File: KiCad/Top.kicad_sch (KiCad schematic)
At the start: 7 parts, among them U143 PZ254V-11-04P_C2691448, U144 HS96L03W2C03

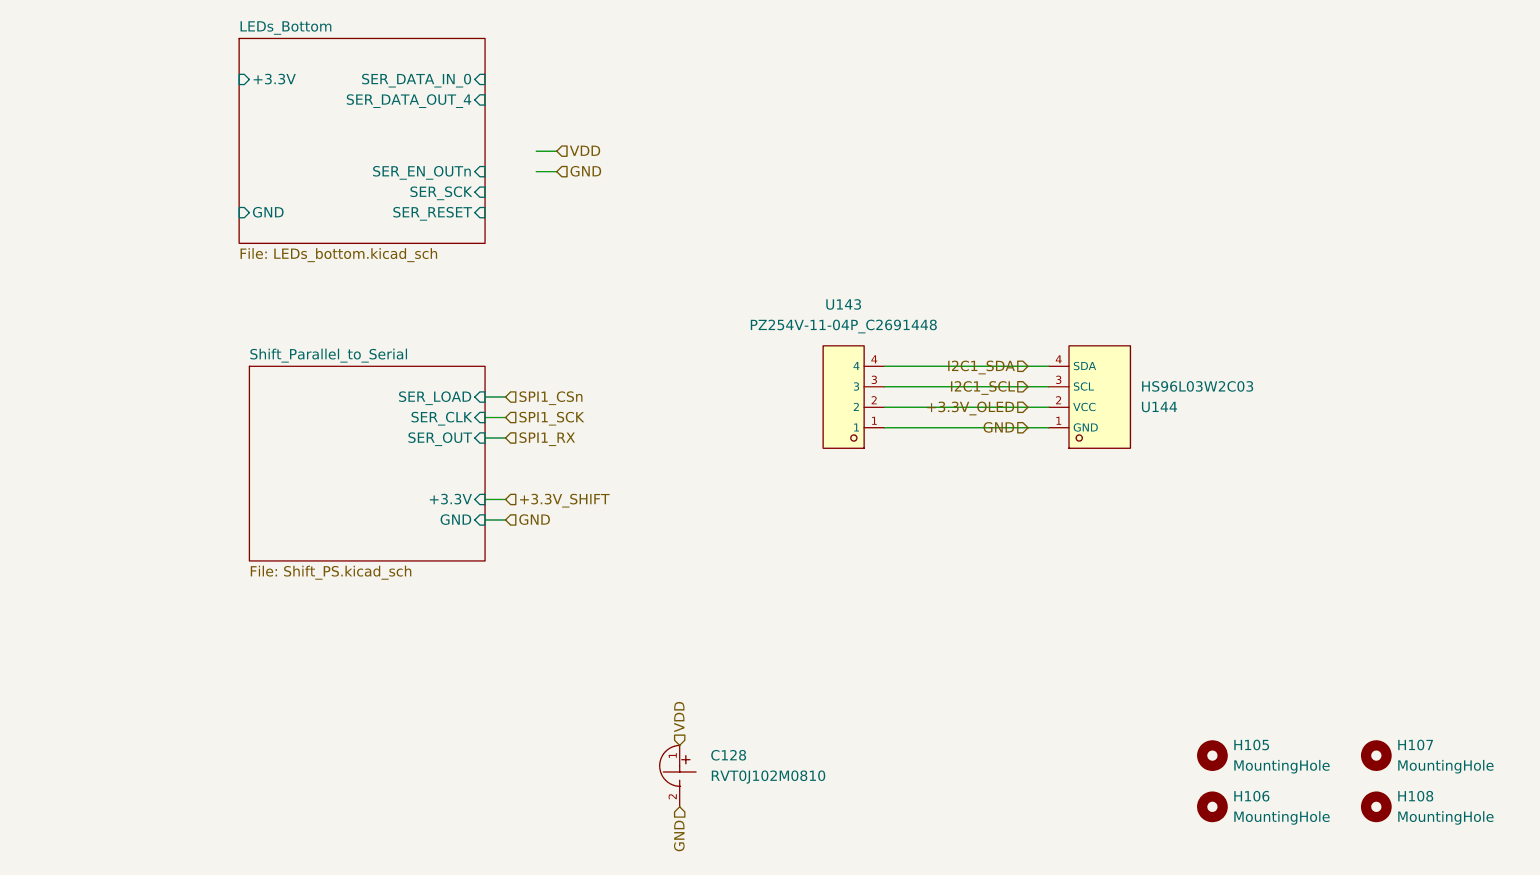
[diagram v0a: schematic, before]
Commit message: Ready for PCB layout with discreet LEDs
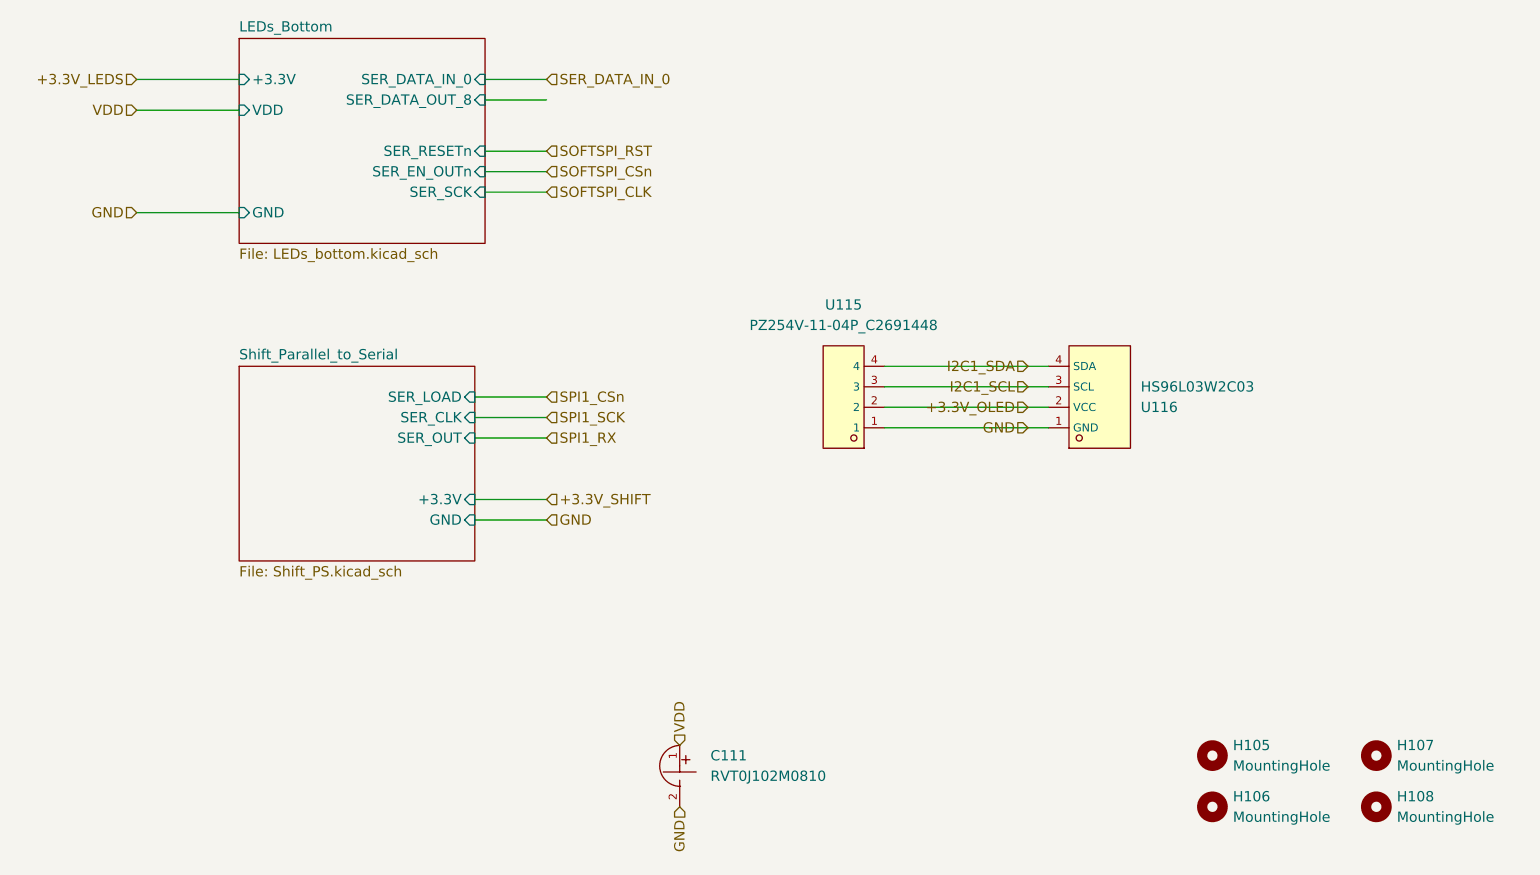
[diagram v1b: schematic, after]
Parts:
- renumbered C128 to C111, U143 to U115, U144 to U116
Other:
- sheet LEDs_Bottom ports: added SER_DATA_OUT_8, SER_RESETn, VDD; removed SER_DATA_OUT_4, SER_RESET
